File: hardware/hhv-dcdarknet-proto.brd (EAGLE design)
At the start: 43.2 x 59.7 mm, 29 parts

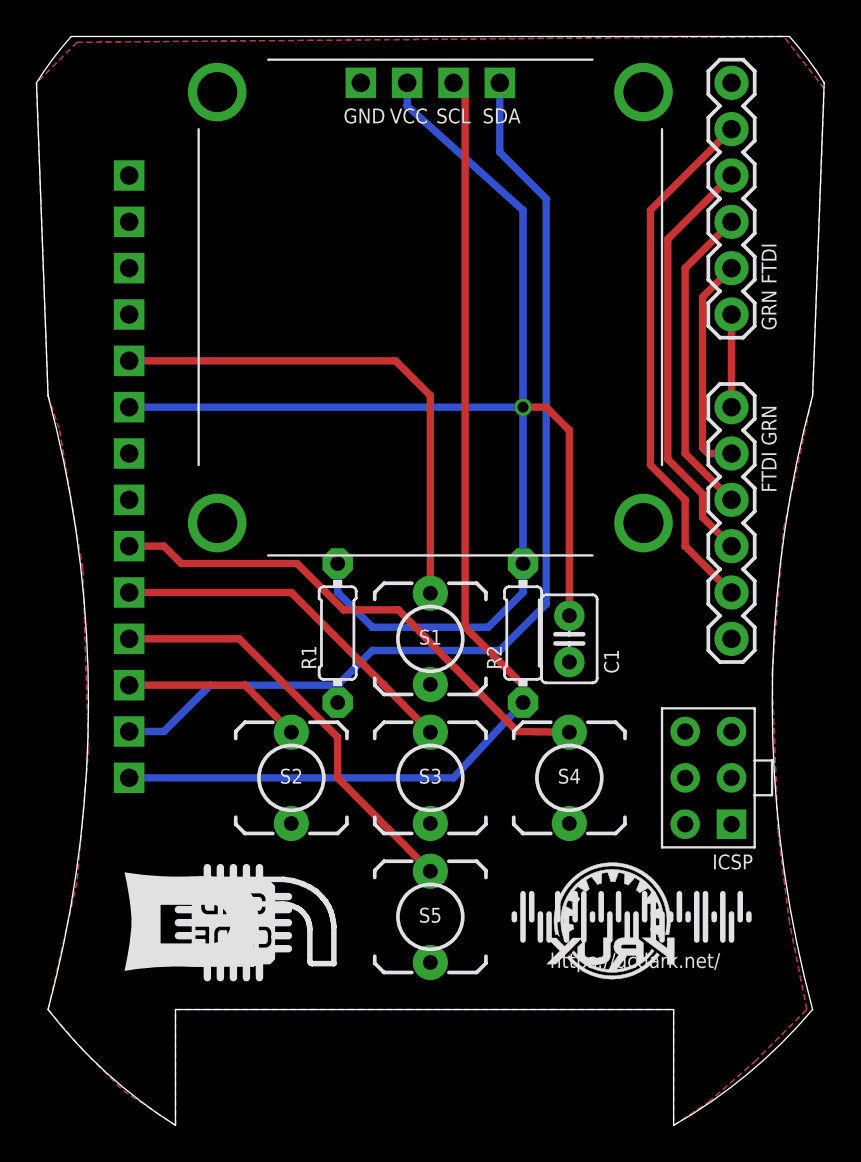
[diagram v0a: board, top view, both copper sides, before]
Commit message: Updated Eagle files for the 2015 boards.
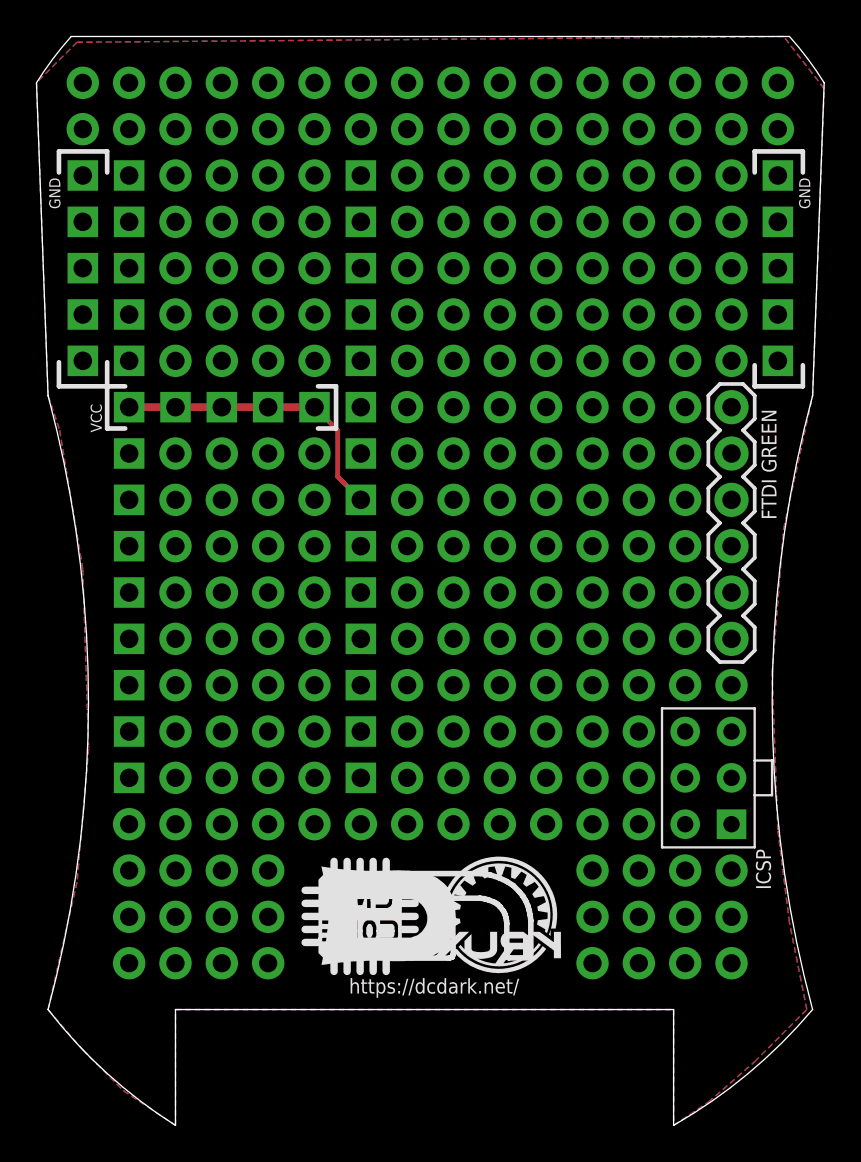
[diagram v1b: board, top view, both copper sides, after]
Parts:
- removed C1: .1uF, adafruit:C025-030X050
- removed R1, R2: (no value), SYNShop:0204/7
- removed S1: UP, SYNShop:TACTILE-2PIN
- removed S2: LEFT, SYNShop:TACTILE-2PIN
- removed S3: CENTER, SYNShop:TACTILE-2PIN
- removed S4: RIGHT, SYNShop:TACTILE-2PIN
- removed S5: DOWN, SYNShop:TACTILE-2PIN
- removed U$4: CMDC0DE_LOGO, SYNShop:CMDC0DE
- added JP10, JP11, JP12, JP13, JP14, JP15, JP16, JP31, JP32, JP33, JP34, JP35, JP36, JP37, JP38, JP39, JP4, JP40, JP41, JP42, JP43, JP44, JP5, JP6, JP7, JP8, JP9: (no value), adafruit:1X1-SMALL_CUT
- JP3: value FTDI_BASICPTH -> (none); device SparkFun:FTDI_BASIC -> adafruit:1X1-SMALL_CUT
- U$3: value I2C_0.96_OLEDOLED -> CMDC0DE_LOGO; device SYNShop:I2C_0.96_OLED -> SYNShop:CMDC0DE
- moved U$3 45.9 mm to (60.9, 8.92), flipped to the bottom
- moved JP3 32.5 mm to (61.0, 16.5), turned to 0 degrees
- moved U$2 10.8 mm to (58.4, 6.35)
- moved U$1 6.22 mm to (68.6, 9.06)
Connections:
- removed net N$1: JP2.DTR, JP3.DTR
- removed net N$2: JP2.RXI, JP3.RXI
- removed net N$3: JP2.TXO, JP3.TXO
- removed net N$4: JP2.CTS, JP3.CTS
- new net PIN1: JP3.P$1
- new net PIN10: JP12.P$1
- new net PIN11: JP13.P$1
- new net PIN12: JP14.P$1
- new net PIN13: JP15.P$1
- new net PIN14: JP16.P$1
- new net PIN2: JP4.P$1
- new net PIN3: JP5.P$1
- new net PIN4: JP6.P$1
- new net PIN5: JP7.P$1
- new net PIN6: JP8.P$1
- new net PIN9: JP11.P$1
- net +3V3: now also JP41.P$1, JP42.P$1, JP43.P$1, JP44.P$1, JP9.P$1; no longer C1.1, R1.2, R2.2, U$3.VCC
- net +5V: no longer JP3.VCC
- net GND: now also JP10.P$1, JP31.P$1, JP32.P$1, JP33.P$1, JP34.P$1, JP35.P$1, JP36.P$1, JP37.P$1, JP38.P$1, JP39.P$1, JP40.P$1; no longer C1.2, JP3.GND, S1.P$1, S2.P$1, S3.P$1, S4.P$1, S5.P$1, U$3.GND
- net PIN19: no longer S1.P$2
- net PIN23: no longer S4.P$2
- net PIN24: no longer S3.P$2
- net PIN25: no longer S5.P$2
- net PIN26: no longer S2.P$2
- net PIN27: no longer R1.1, U$3.SDA
- net PIN28: no longer R2.1, U$3.SCL
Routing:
- net PIN28: track 58.9 -> 0.00 mm
- net PIN27: track 56.3 -> 0.00 mm
- net +3V3: track 78.9 -> 26.5 mm, vias 1 -> 0
- net N$4: track 29.1 -> 0.00 mm, vias 0 -> 1
- net PIN23: track 28.4 -> 0.00 mm
- net PIN19: track 28.1 -> 0.00 mm
- net +5V: track 23.2 -> 0.00 mm
- net PIN25: track 23.1 -> 0.00 mm
- net PIN24: track 19.7 -> 0.00 mm
- net N$3: track 17.3 -> 0.00 mm, vias 0 -> 1
- net N$2: track 12.2 -> 0.00 mm, vias 0 -> 1
- net PIN26: track 9.97 -> 0.00 mm
- net N$1: track 5.08 -> 0.00 mm, vias 0 -> 1
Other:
- board text added: "Assembly: DN-PRTBD Rev 1.0"
- board text added: "FTDI GREEN"
- board text removed: "Assembly: DN-DISPBRD Rev 1.03"
- board text removed: "FTDI GRN"
- board text removed: "GRN FTDI"
- board text removed: "SCL"
- board text removed: "SDA"
